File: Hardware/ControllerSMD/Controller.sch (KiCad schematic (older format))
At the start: 61 parts, among them J1 8P8C, J2 LCD Header, J3 USB_B_Micro, J4 S88, J5 Screw_Terminal_01x05, SW1 Rotary_Encoder_Switch, SW2 SW_F0, SW3 SW_F1, SW4 SW_F2, SW5 SW_F3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

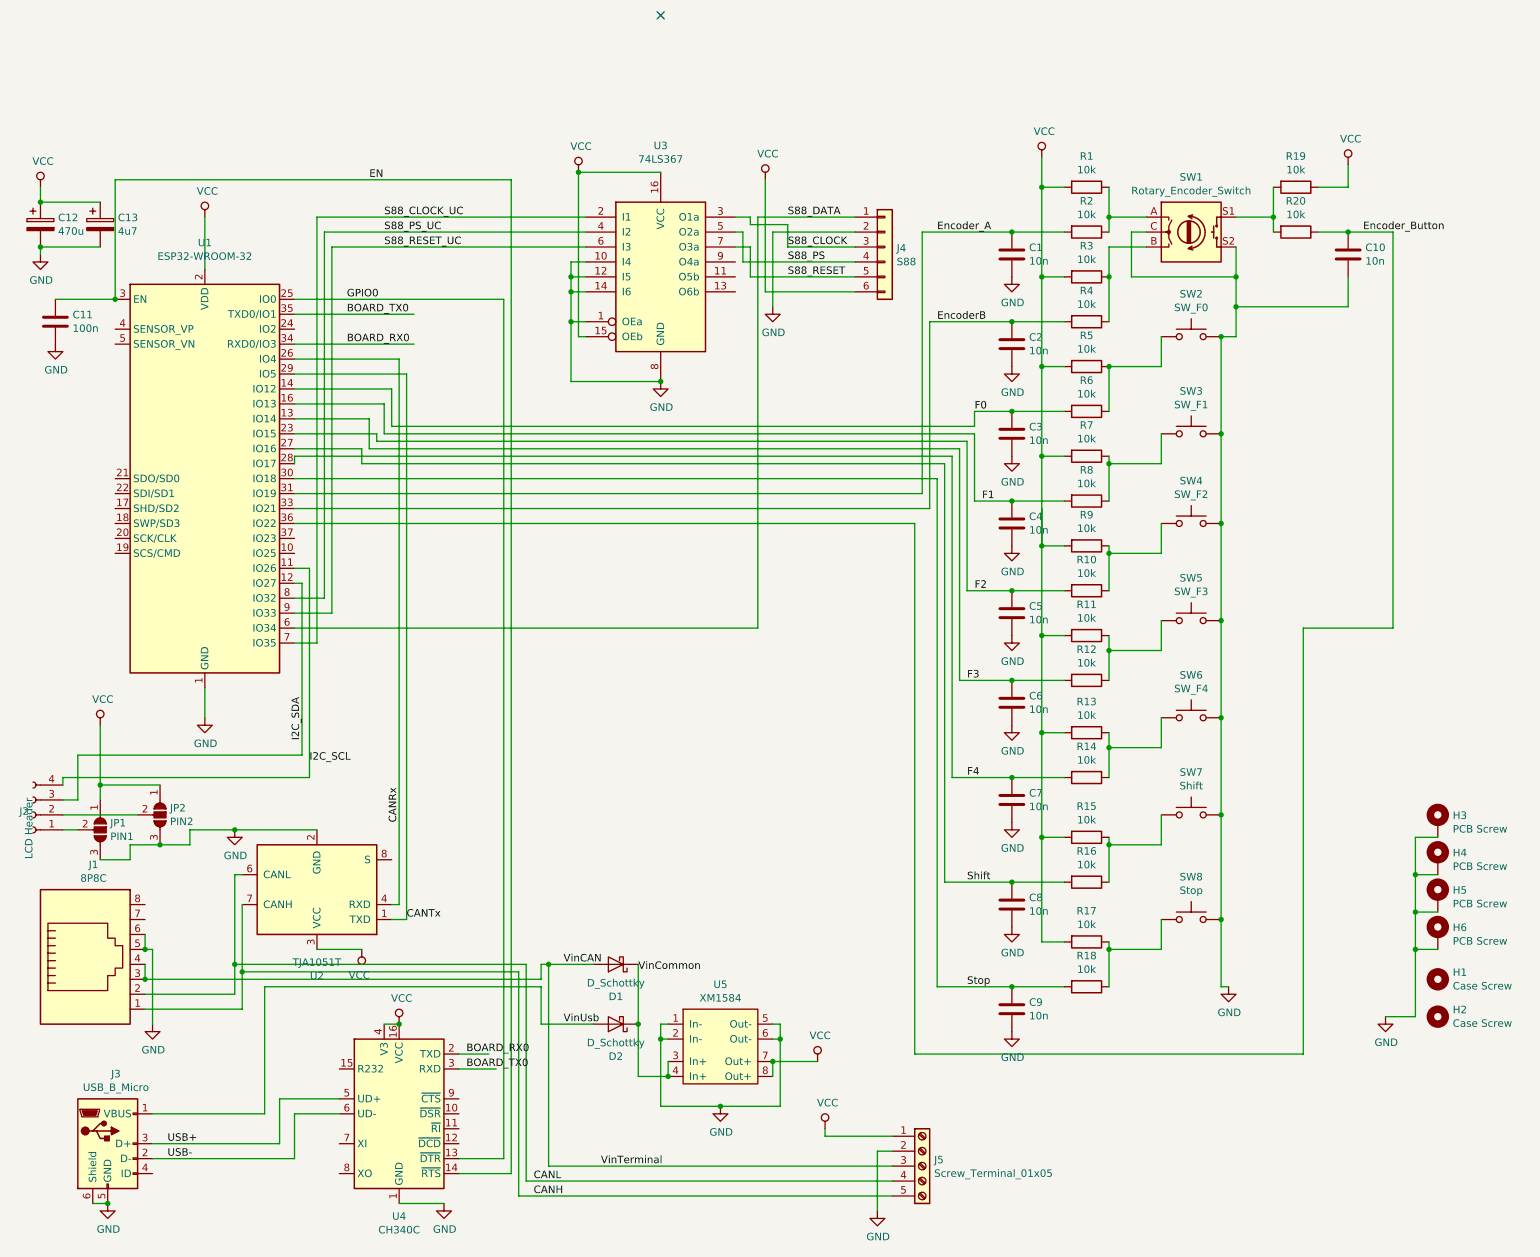
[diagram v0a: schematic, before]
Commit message: Updated all boards
ESP32Breakout now with S88 driver.
ESP32Breakout has the auto-reset circut removed.
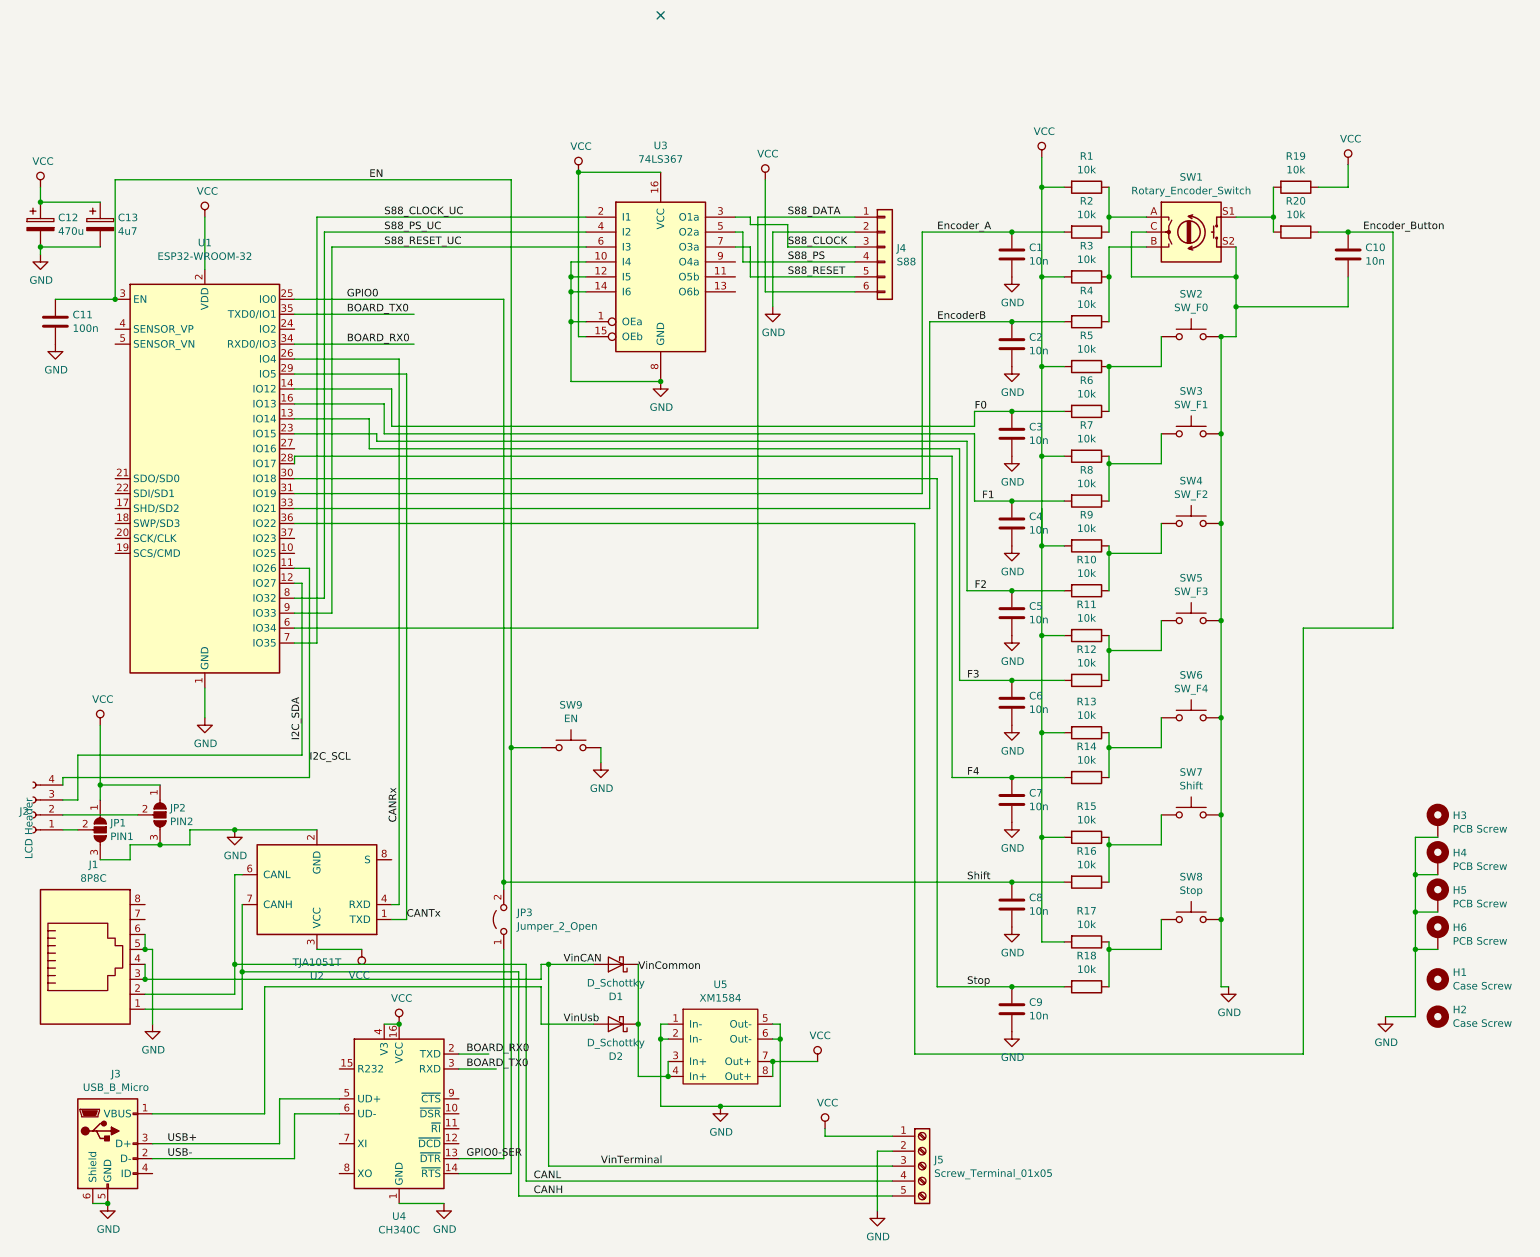
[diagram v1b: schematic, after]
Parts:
- added JP3: Jumper_2_Open, Jumper:SolderJumper-2_P1.3mm_Open_Pad1.0x1.5mm, symbol Jumper:Jumper_2_Open
- added SW9: EN, Button_Switch_SMD:SW_Push_1P1T_NO_CK_KMR2, symbol Switch:SW_Push
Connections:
- net EN: now also SW9.1
- net GND: now also SW9.2
- net GPIO0: now also C8.2, R16.2, JP3.2 (B); no longer U4.13 (~DTR)
- removed net Shift: C8.2, R16.2, U1.27 (IO16)
- new net GPIO0-SER: JP3.1 (A), U4.13 (~DTR)
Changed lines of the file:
@@
 EESchema Schematic File Version 4
 LIBS:Controller-cache
-EELAYER 26 0
+EELAYER 29 0
 EELAYER END
 $Descr A4 11693 8268
@@
 	6750 4700 7150 4700
 Connection ~ 7150 4700
-Wire Wire Line
-	6700 2600 6700 5400
-Wire Wire Line
-	6700 5400 7150 5400
 Connection ~ 7150 5400
 Wire Wire Line
@@
 	3450 7350 3800 7350
 Wire Wire Line
-	3800 7350 3800 700
+	3800 7350 3800 4500
 Wire Wire Line
 	3800 700  1150 700
@@
 Wire Wire Line
 	3450 7250 3750 7250
-Wire Wire Line
-	3750 7250 3750 1500
 Wire Wire Line
 	3750 1500 2350 1500
@@
 	2350 2550 6750 2550
 Wire Wire Line
-	2350 2500 2800 2500
-Wire Wire Line
-	2800 2500 2800 2600
-Wire Wire Line
-	2800 2600 6700 2600
-Wire Wire Line
 	2600 3600 2350 3600
 Wire Wire Line
@@
 Text Label 3500 6550 0    50   ~ 0
 BOARD_RX0
+Wire Wire Line
+	3750 5400 7150 5400
+Wire Wire Line
+	3750 5400 3750 1500
+$Comp
+L Switch:SW_Push SW9
+U 1 1 5E0598C5
+P 4200 4500
+F 0 "SW9" H 4200 4785 50  0000 C CNN
+F 1 "EN" H 4200 4694 50  0000 C CNN
+F 2 "Button_Switch_SMD:SW_Push_1P1T_NO_CK_KMR2" H 4200 4700 50  0001 C CNN
+F 3 "" H 4200 4700 50  0001 C CNN
+	1    4200 4500
+	1    0    0    -1
+$EndComp
+$Comp
+L power:GND #PWR0134
+U 1 1 5E05A3A3
+P 4400 4600
+F 0 "#PWR0134" H 4400 4350 50  0001 C CNN
+F 1 "GND" H 4405 4427 50  0000 C CNN
+F 2 "" H 4400 4600 50  0001 C CNN
+F 3 "" H 4400 4600 50  0001 C CNN
+	1    4400 4600
+	1    0    0    -1
+$EndComp
+Wire Wire Line
+	4000 4500 3800 4500
+Connection ~ 3800 4500
+Wire Wire Line
+	3800 4500 3800 700
+Wire Wire Line
+	4400 4500 4400 4600
+$Comp
+L Jumper:Jumper_2_Open JP3
+U 1 1 5E08CDE3
+P 3750 5650
+F 0 "JP3" V 3796 5562 50  0000 R CNN
+F 1 "Jumper_2_Open" V 3705 5562 50  0000 R CNN
+F 2 "Jumper:SolderJumper-2_P1.3mm_Open_Pad1.0x1.5mm" H 3750 5650 50  0001 C CNN
+F 3 "~" H 3750 5650 50  0001 C CNN
+	1    3750 5650
+	0    -1   -1   0
+$EndComp
+Wire Wire Line
+	3750 5400 3750 5450
+Connection ~ 3750 5400
+Wire Wire Line
+	3750 7250 3750 5850
+Text Label 3500 7250 0    50   ~ 0
+GPIO0-SER
 $EndSCHEMATC
